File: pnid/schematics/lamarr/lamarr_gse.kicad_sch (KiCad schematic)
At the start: 20 parts

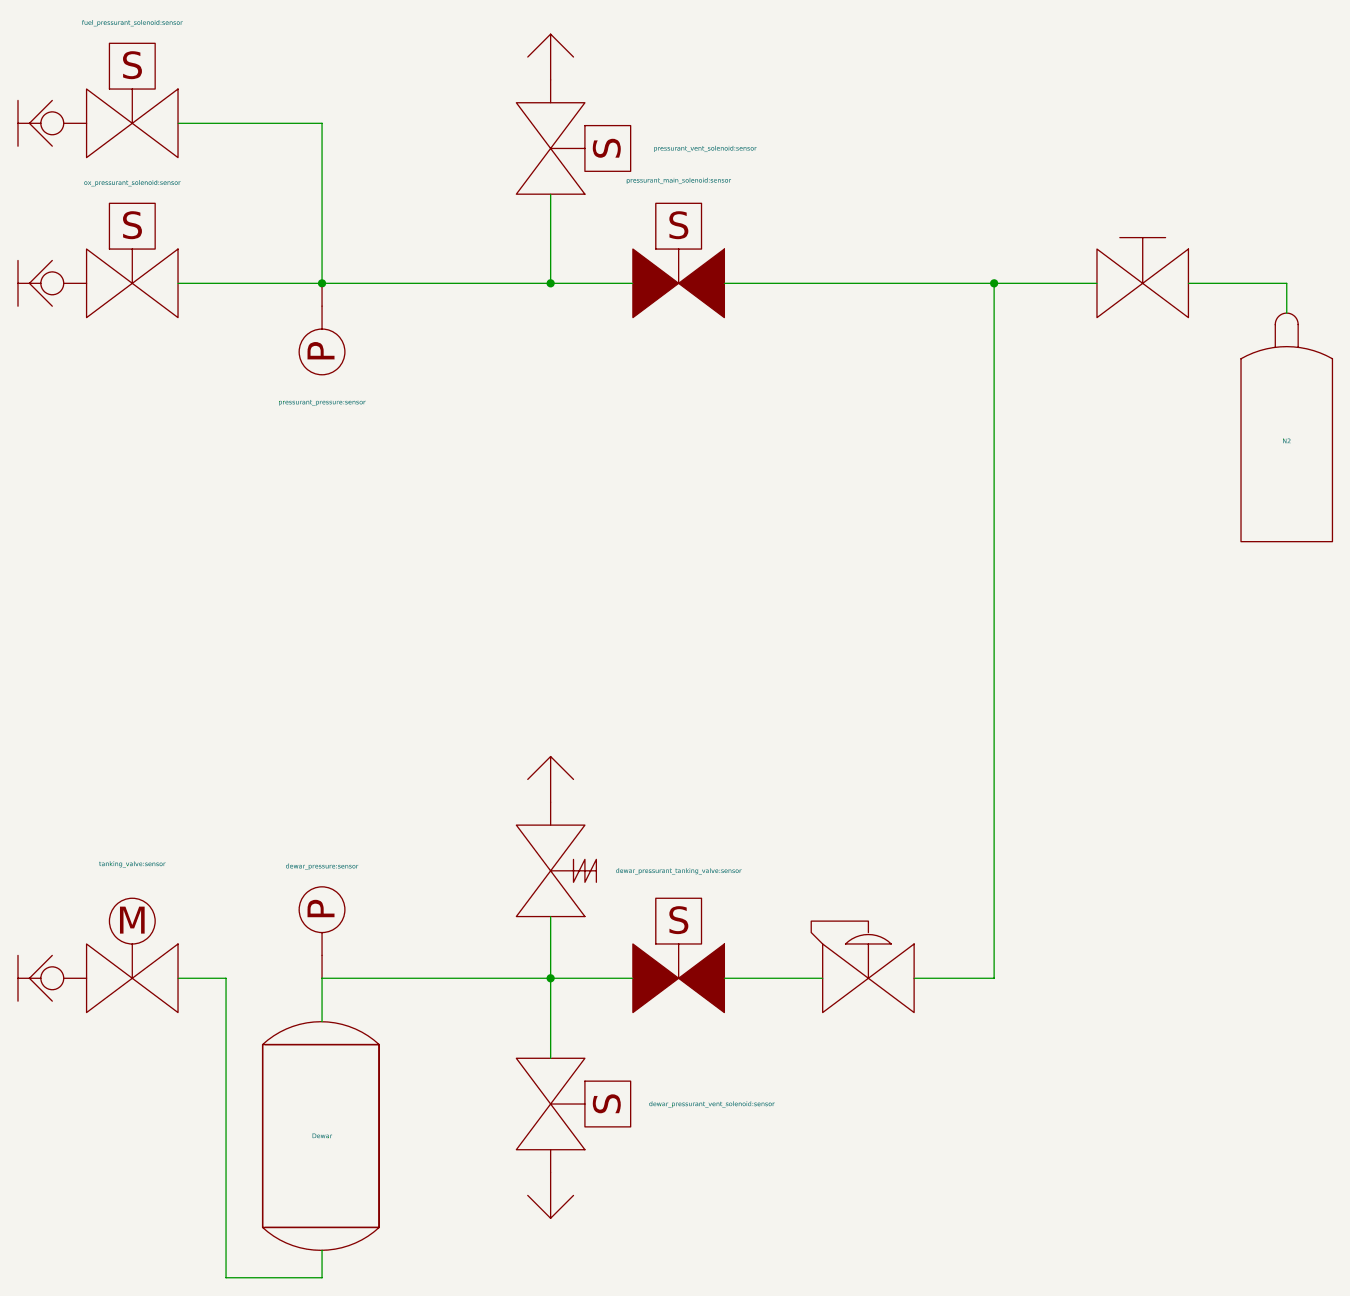
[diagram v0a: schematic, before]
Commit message: improve label placement for remaining pnids
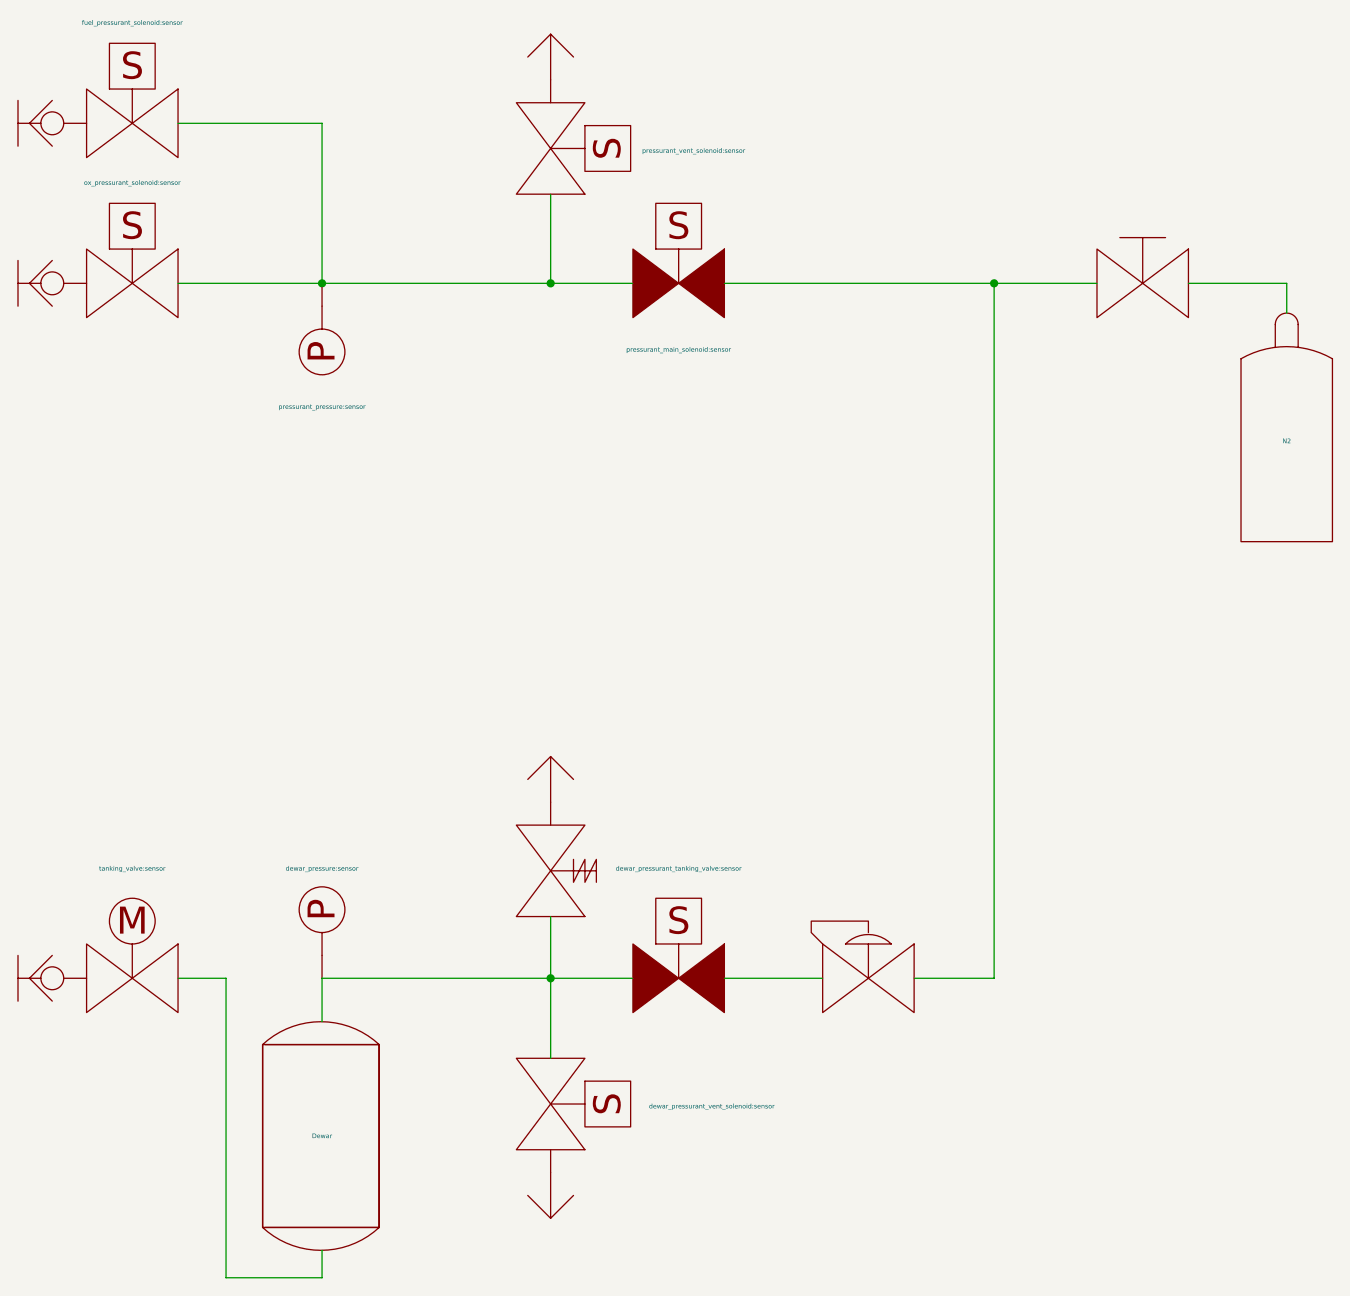
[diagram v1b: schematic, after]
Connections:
- new net: DewarPressureRegulator.~, ManualN2BottleValve.~, pressurant_main_solenoid.~
- new net: Dewar.~, DewarOverPressureValve.~, dewar_pressurant_tanking_valve.~, dewar_pressurant_vent_solenoid.~, dewar_pressure.~
- new net: fuel_pressurant_solenoid.~, ox_pressurant_solenoid.~, pressurant_main_solenoid.~, pressurant_pressure.~, pressurant_vent_solenoid.~
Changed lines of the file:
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@@
 		)
 		(property "Value" "dewar_pressurant_tanking_valve:sensor"
-			(at 102.362 122.174 0)
+			(at 102.362 121.92 0)
 			(effects
 				(font
@@
 		)
 		(property "Value" "dewar_pressurant_vent_solenoid:sensor"
-			(at 99.06 148.082 90)
+			(at 99.06 148.336 90)
 			(effects
 				(font
@@
 		)
 		(property "Value" "dewar_pressure:sensor"
-			(at 62.738 121.666 90)
+			(at 62.738 121.92 90)
 			(effects
 				(font
@@
 		)
 		(property "Value" "tanking_valve:sensor"
-			(at 41.656 121.412 0)
+			(at 41.656 121.92 0)
 			(effects
 				(font
@@
 		)
 		(property "Value" "pressurant_main_solenoid:sensor"
-			(at 102.362 45.466 0)
+			(at 102.362 64.262 0)
 			(effects
 				(font
@@
 		)
 		(property "Value" "pressurant_vent_solenoid:sensor"
-			(at 99.568 41.91 90)
+			(at 98.298 42.164 90)
 			(effects
 				(font
@@
 		)
 		(property "Value" "pressurant_pressure:sensor"
-			(at 62.738 70.104 90)
+			(at 62.738 70.612 90)
 			(effects
 				(font
@@
 	)
 	(symbol
-		(lib_name "PnID-Lib:Valve_Solenoid_NO")
 		(lib_id "PnID-Lib:Valve_Solenoid_NO")
 		(at 41.656 39.116 0)
@@
 	)
 	(symbol
-		(lib_name "PnID-Lib:Valve_Solenoid_NO")
 		(lib_id "PnID-Lib:Valve_Solenoid_NO")
 		(at 41.656 56.896 0)
